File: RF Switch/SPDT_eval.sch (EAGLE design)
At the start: 10 parts, among them J1 142-0711-821, J2 142-0711-821, J3 142-0711-821, J4 22-23-2051, U1 QPC1022

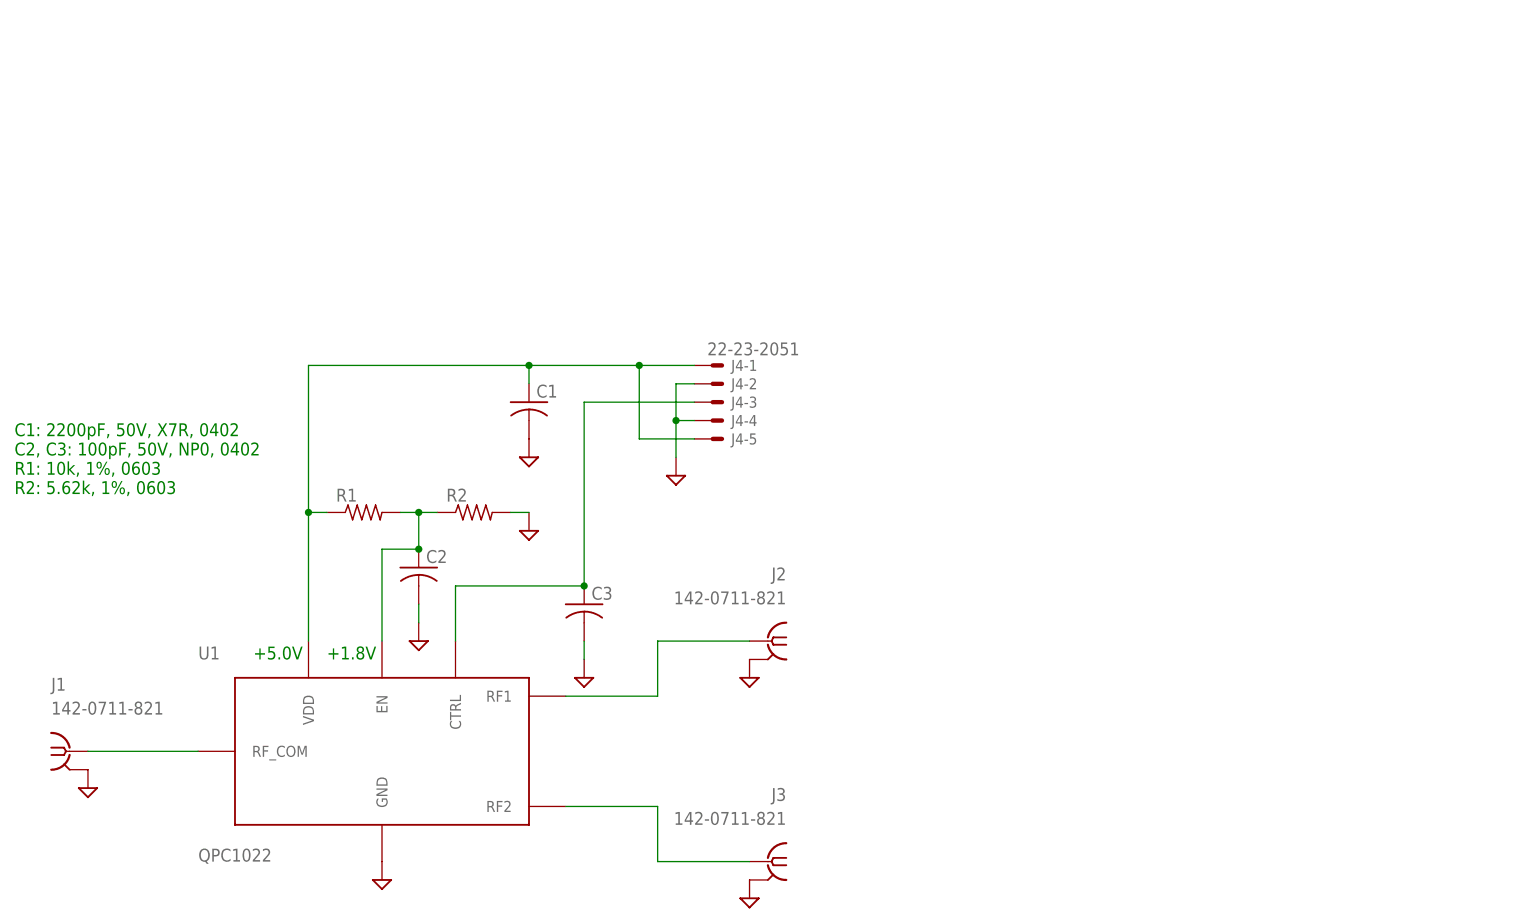
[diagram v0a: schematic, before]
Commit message: Cleaned up SPDT switch evaluation board. Same as filter, cleaned up lots of EAGLE stuff. - 10 mil grid, snapped to grid. - Replaced SMA conectors - RF class added. - OSH park 2 layer (4 LAYER?!) DRC used. - Added frame and added names to signals. - Added board name.
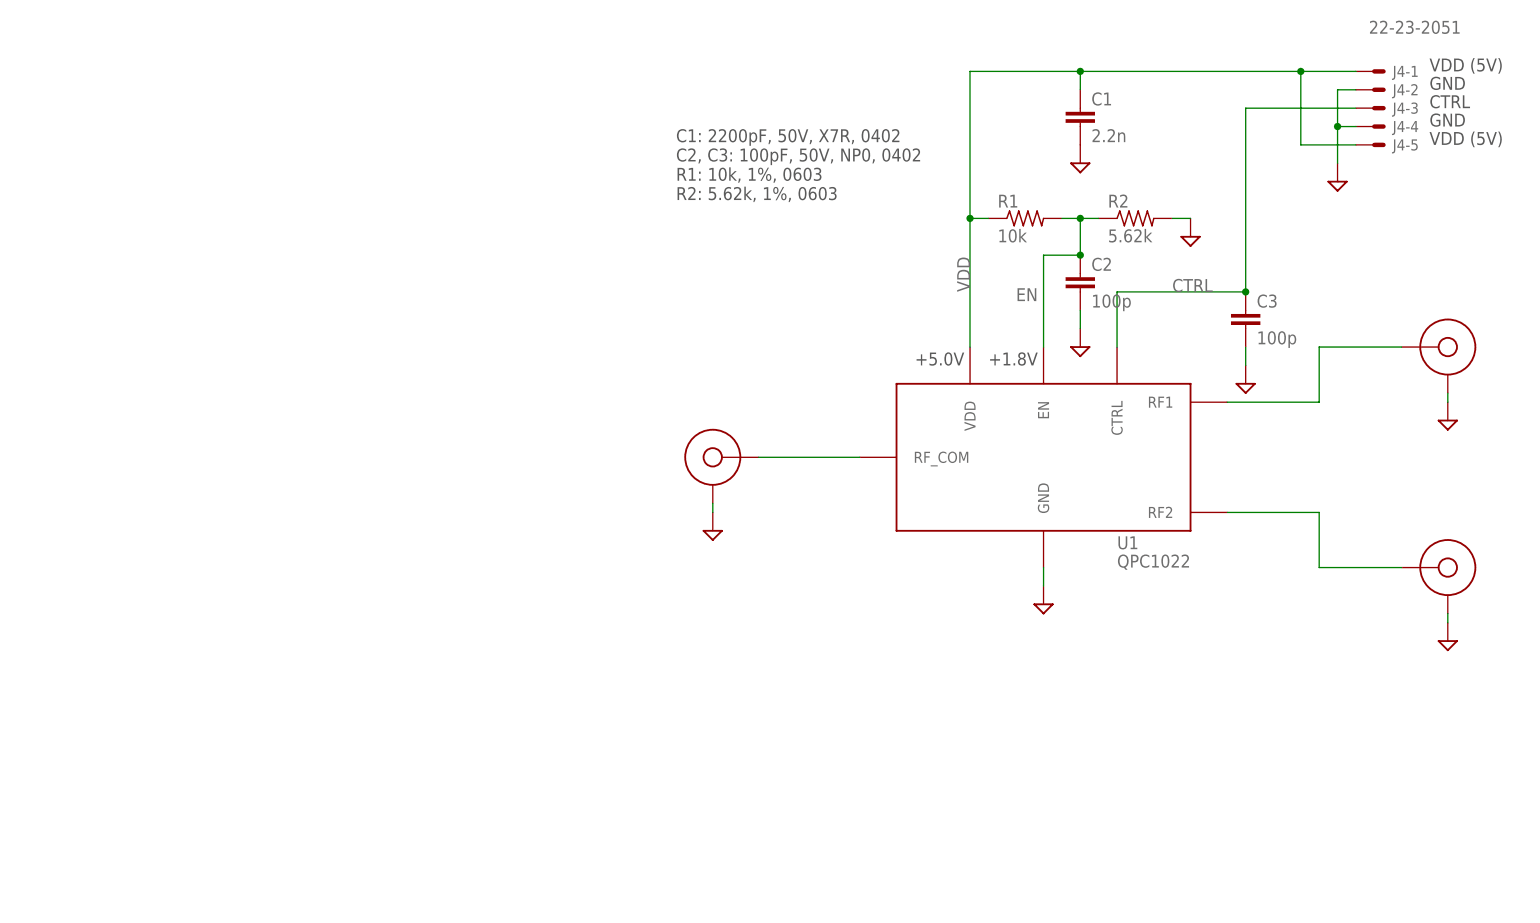
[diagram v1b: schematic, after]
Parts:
- removed J1, J2, J3: 142-0711-821, con-coax:SMA-142-0711-821/826
- added CF1, CF2, CF3: SMA-CINCH-END-FIRE, psas_c3_team05:SMA-CINCH-END-FIRE
- C1: value (none) -> 2.2n; device rcl:C-USC0402 -> rcl_custom:C-EU0402-B-NOSILK
- C2, C3: value (none) -> 100p; device rcl:C-USC0402 -> rcl_custom:C-EU0402-B-NOSILK
- R1: value (none) -> 10k; device rcl:R-US_R0603 -> rcl_custom:R-US_0603-B-NOSILK
- R2: value (none) -> 5.62k; device rcl:R-US_R0603 -> rcl_custom:R-US_0603-B-NOSILK
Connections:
- net N$4 renamed VDD
- net N$5 renamed EN
- net N$7 renamed CTRL
- removed net N$1: J1.1, U1.RF_COM
- removed net N$2: J2.1, U1.RF1
- removed net N$3: J3.1, U1.RF2
- new net COM: CF1.CENTERCONDUCTOR, U1.RF_COM
- new net RF1: CF2.CENTERCONDUCTOR, U1.RF1
- new net RF2: CF3.CENTERCONDUCTOR, U1.RF2
- net GND: now also CF1.GND, CF2.GND, CF3.GND; no longer J1.2, J2.2, J3.2
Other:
- note added: "CTRL"
- note added: "GND"
- note added: "VDD (5V)"
- moved on the sheet: J4-1, J4-2, J4-3, J4-4, J4-5, U1
